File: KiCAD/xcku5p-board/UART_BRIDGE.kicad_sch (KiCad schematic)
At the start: 7 parts

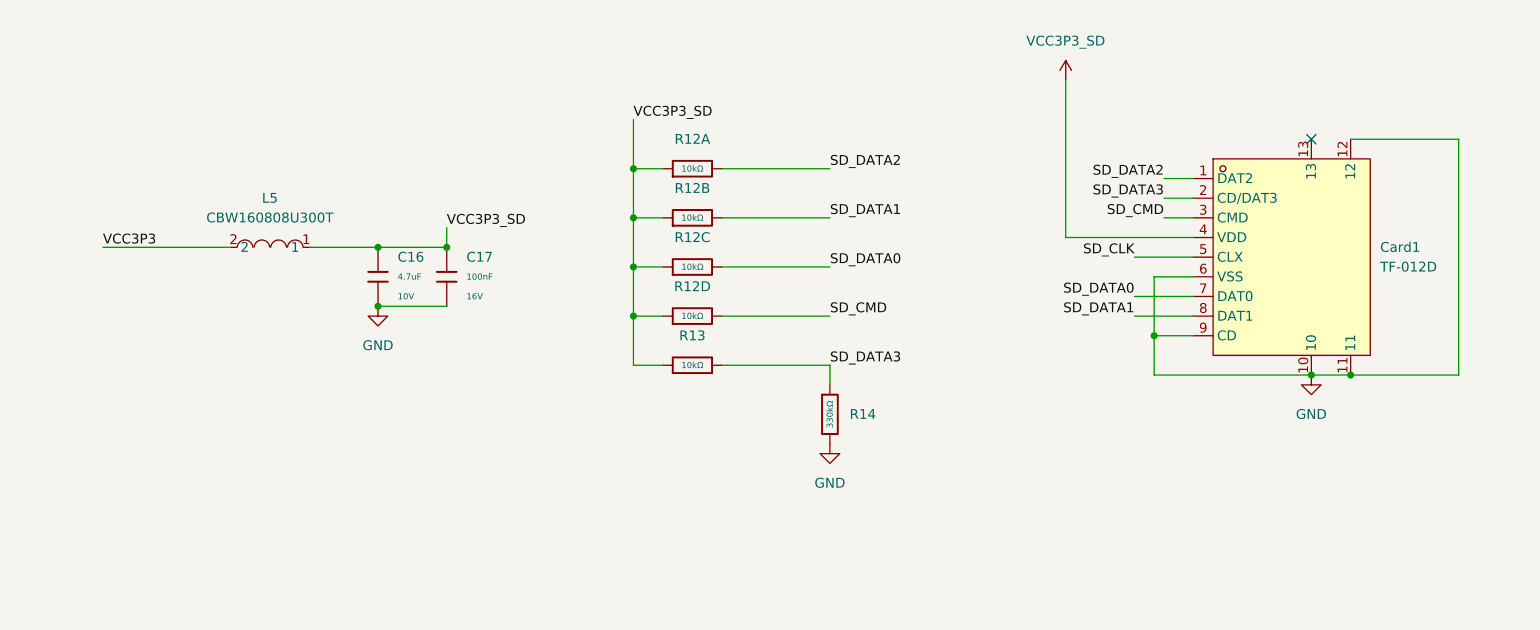
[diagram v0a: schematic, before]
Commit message: Add power circuit, switches, UART bridge
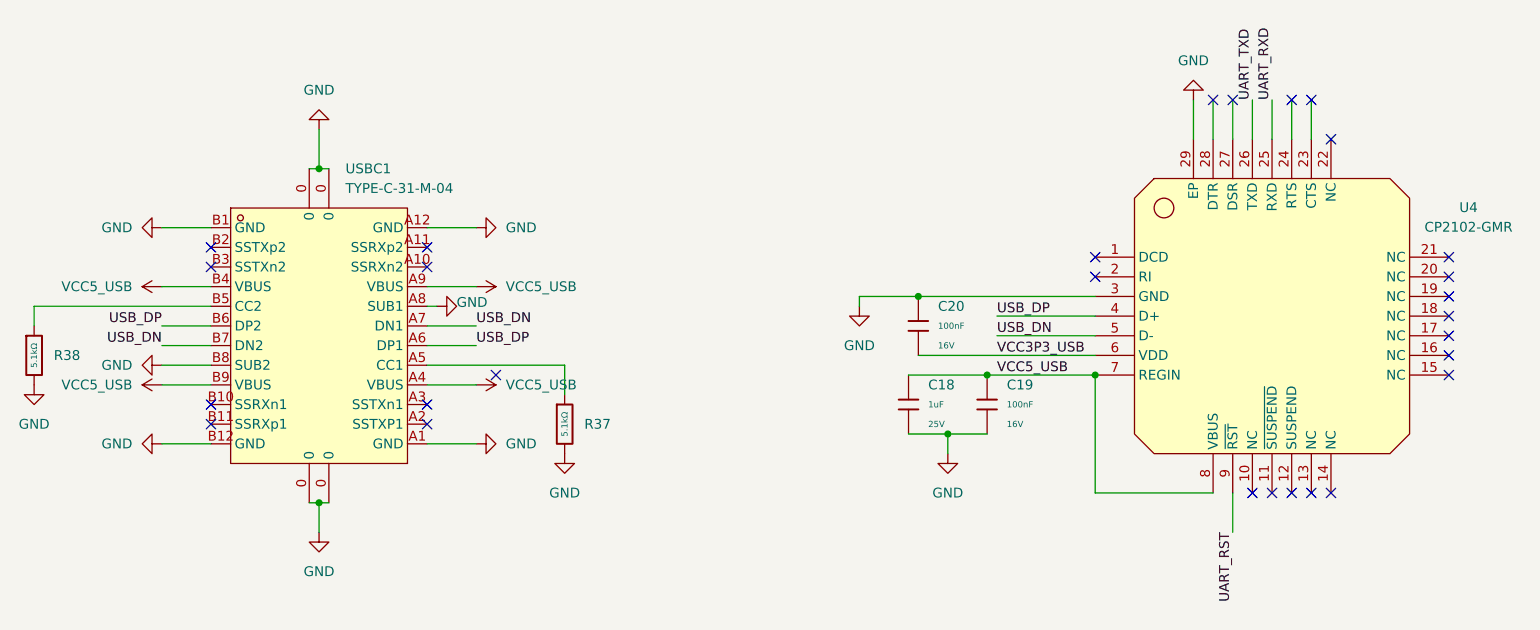
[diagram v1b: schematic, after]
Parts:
- removed C16: 4.7uF, PCM_JLCPCB:C_0402, symbol PCM_JLCPCB-Capacitors:0402,4.7uF
- removed C17: 100nF, PCM_JLCPCB:C_0402, symbol PCM_JLCPCB-Capacitors:0402,100nF
- removed Card1: TF-012D, easyeda2kicad:TF-SMD_TF-012, symbol easyeda2kicad:TF-012D
- removed L5: CBW160808U300T, easyeda2kicad:L0603, symbol easyeda2kicad:CBW160808U300T
- removed R12: 10kΩ, PCM_JLCPCB:R_0402x4, symbol PCM_JLCPCB-Resistors:0402x4,10kΩ
- removed R13: 10kΩ, PCM_JLCPCB:R_0402, symbol PCM_JLCPCB-Resistors:0402,10kΩ
- removed R14: 330kΩ, PCM_JLCPCB:R_0402, symbol PCM_JLCPCB-Resistors:0402,330kΩ
- added C18: 1uF, PCM_JLCPCB:C_0402, symbol PCM_JLCPCB-Capacitors:0402,1uF
- added C19, C20: 100nF, PCM_JLCPCB:C_0402, symbol PCM_JLCPCB-Capacitors:0402,100nF
- added R37, R38: 5.1kΩ, PCM_JLCPCB:R_0402, symbol PCM_JLCPCB-Resistors:0402,5.1kΩ
- added U4: CP2102-GMR, easyeda2kicad:WQFN-28_L5.0-W5.0-P0.50-BL-EP3.2, symbol easyeda2kicad:CP2102-GMR
- added USBC1: TYPE-C-31-M-04, easyeda2kicad:USB-C-SMD_TYPE-C-USB-20, symbol easyeda2kicad:TYPE-C-31-M-04
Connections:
- net GND: now also C18.2, C19.2, C20.1, R37.2, R38.2, U4.29 (EP), U4.3 (GND), USBC1.0, USBC1.A1 (GND), USBC1.A12 (GND), USBC1.A8 (SUB1), USBC1.B1 (GND), USBC1.B12 (GND), USBC1.B8 (SUB2)
- new net: R38.1, USBC1.B5 (CC2)
- new net: R37.1, USBC1.A5 (CC1)
- new net UART_RST: U4.9 (~{RST})
- new net UART_RXD: U4.25 (RXD)
- new net UART_TXD: U4.26 (TXD)
- new net USB_DN: U4.5 (D-), USBC1.A7 (DN1), USBC1.B7 (DN2)
- new net USB_DP: U4.4 (D+), USBC1.A6 (DP1), USBC1.B6 (DP2)
- new net VCC3P3_USB: C20.2, U4.6 (VDD)
- new net VCC5_USB: C18.1, C19.1, U4.7 (REGIN), U4.8 (VBUS), USBC1.A4 (VBUS), USBC1.A9 (VBUS), USBC1.B4 (VBUS), USBC1.B9 (VBUS)
- no-connect marks 1 -> 28
